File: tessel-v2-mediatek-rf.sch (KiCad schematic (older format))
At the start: 41 parts, among them J501 CONN_01X01, J502 CONN_01X01, T501 2450BL15B100, T502 2450BL15B100, U201 MT7620N

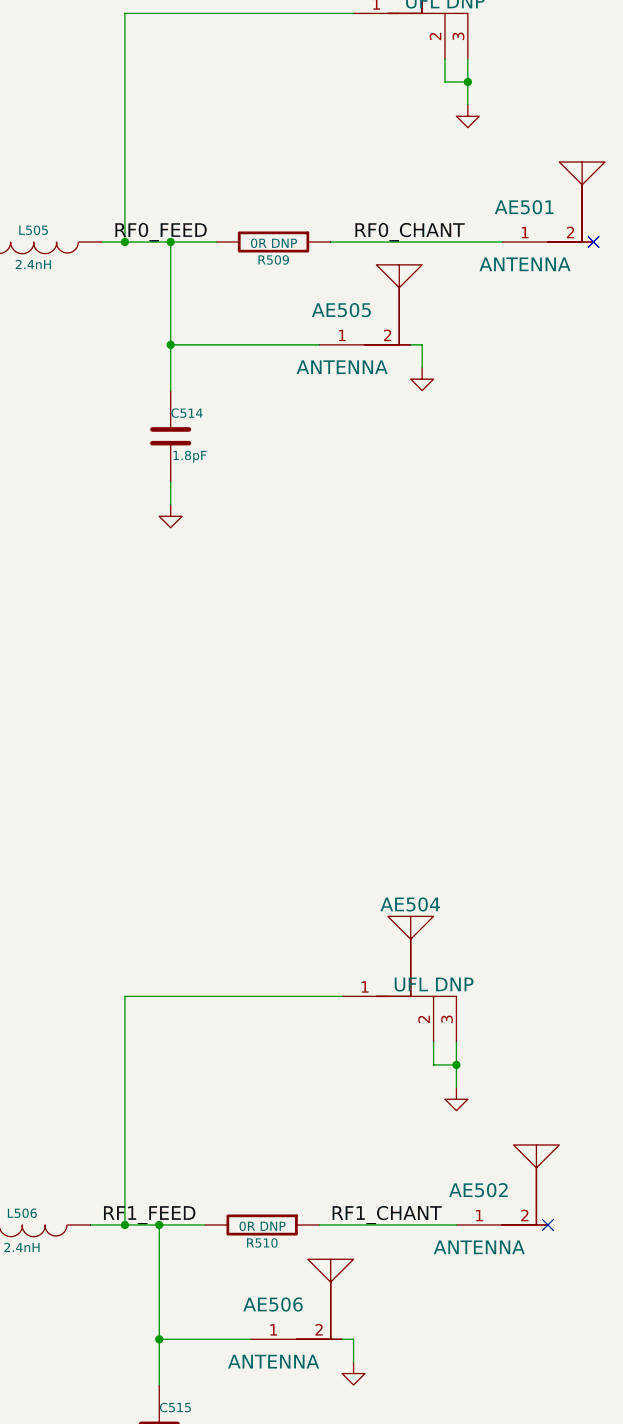
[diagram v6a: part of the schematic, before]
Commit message: removed chip antennas. made ground planes.
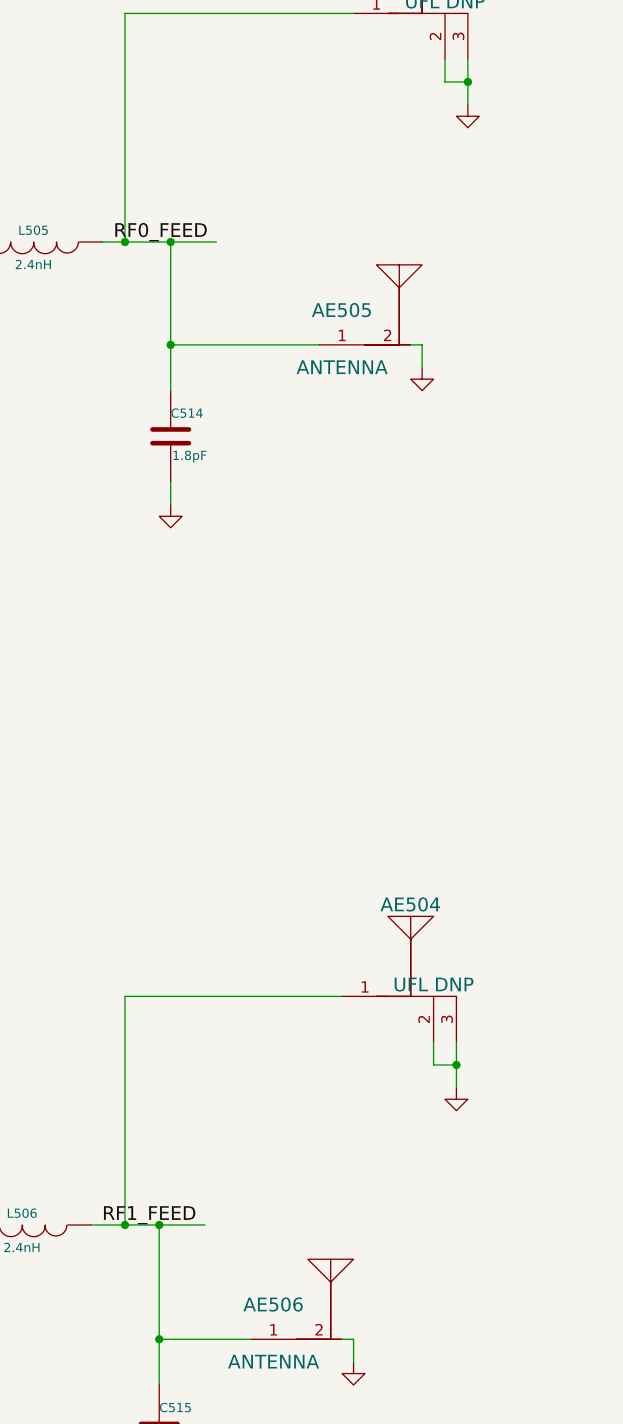
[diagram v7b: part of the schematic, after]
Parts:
- removed AE501, AE502: ANTENNA, tm-kicad-lib:ANTENNA-SMT-2.45GHz, symbol ANTENNA
- removed R509, R510: 0R DNP, tm-kicad-lib:SMD-0402, symbol R
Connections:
- no-connect marks 4 -> 2
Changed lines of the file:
@@
-$EndComp
-$Comp
-L ANTENNA AE501
-U 1 1 5491EF9D
-P 13400 3300
-F 0 "AE501" H 13400 3450 60  0000 C CNN
-F 1 "ANTENNA" H 13400 3200 60  0000 C CNN
-F 2 "tm-kicad-lib:ANTENNA-SMT-2.45GHz" H 13500 3300 60  0001 C CNN
-F 3 "" H 13500 3300 60  0000 C CNN
-	1    13400 3300
-	1    0    0    -1
 $EndComp
 $Comp
@@
 $EndComp
 $Comp
-L ANTENNA AE502
-U 1 1 5492F389
-P 13200 7600
-F 0 "AE502" H 13200 7750 60  0000 C CNN
-F 1 "ANTENNA" H 13200 7500 60  0000 C CNN
-F 2 "tm-kicad-lib:ANTENNA-SMT-2.45GHz" H 13300 7600 60  0001 C CNN
-F 3 "" H 13300 7600 60  0000 C CNN
-	1    13200 7600
-	1    0    0    -1
-$EndComp
-$Comp
 L UFL AE504
 U 1 1 5492F38F
@@
 	-1   0    0    1
 $EndComp
-NoConn ~ 13700 3300
-NoConn ~ 13500 7600
 Text Label 3750 4850 0    60   ~ 0
 ANT_TRN
@@
 $EndComp
 $Comp
-L R R509
-U 1 1 54BF2178
-P 12300 3300
-F 0 "R509" V 12380 3300 40  0000 C CNN
-F 1 "0R DNP" V 12307 3301 40  0000 C CNN
-F 2 "tm-kicad-lib:SMD-0402" V 12230 3300 30  0001 C CNN
-F 3 "" H 12300 3300 30  0000 C CNN
-	1    12300 3300
-	0    1    1    0
-$EndComp
-Text Label 12650 3300 0    60   ~ 0
-RF0_CHANT
-$Comp
 L ANTENNA AE506
 U 1 1 54BF2584
@@
 	1    0    0    -1
 $EndComp
-$Comp
-L R R510
-U 1 1 54BF2592
-P 12250 7600
-F 0 "R510" V 12330 7600 40  0000 C CNN
-F 1 "0R DNP" V 12257 7601 40  0000 C CNN
-F 2 "tm-kicad-lib:SMD-0402" V 12180 7600 30  0001 C CNN
-F 3 "" H 12250 7600 30  0000 C CNN
-	1    12250 7600
-	0    1    1    0
-$EndComp
-Text Label 12550 7600 0    60   ~ 0
-RF1_CHANT
 Text Label 7900 7450 0    60   ~ 0
 RF1_BALUN_IN_P
@@
 	9000 3300 9050 3300
 Wire Wire Line
-	12500 7600 13100 7600
-Wire Wire Line
-	12550 3300 13300 3300
-Wire Wire Line
 	5650 3150 5650 3250
